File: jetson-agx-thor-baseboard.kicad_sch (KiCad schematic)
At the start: 7 parts

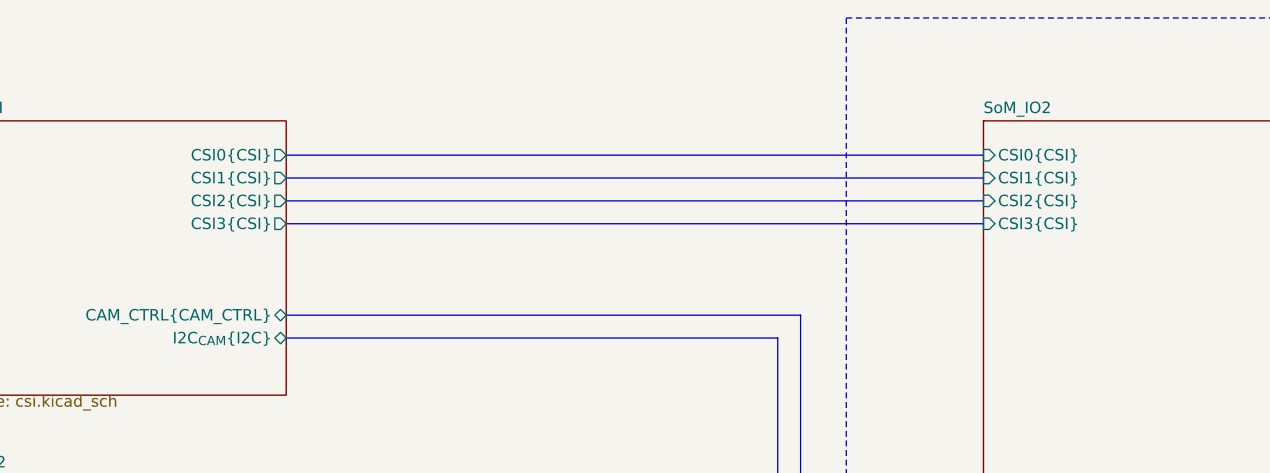
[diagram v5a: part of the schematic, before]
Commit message: [#85326] Update CSI naming convention
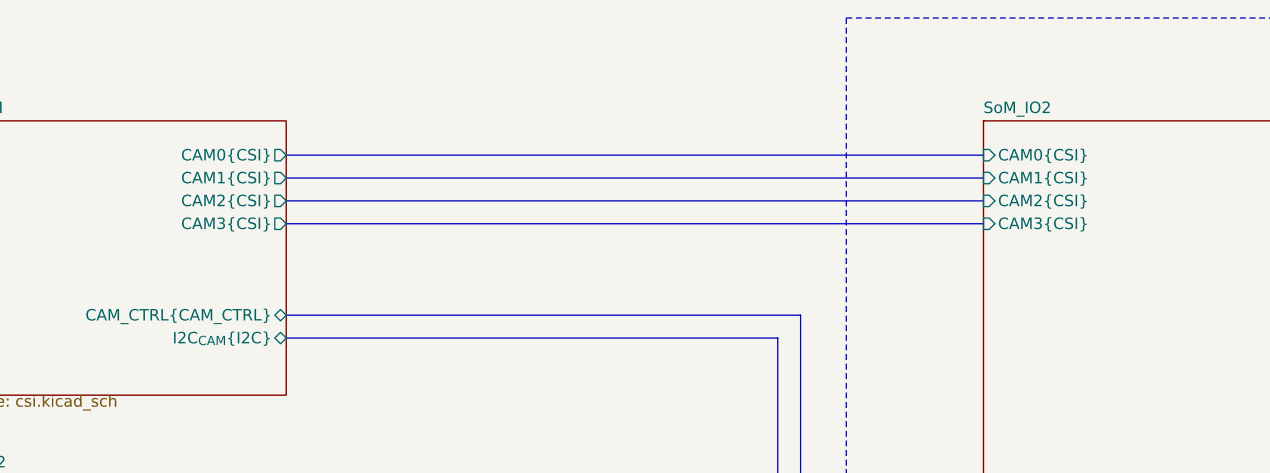
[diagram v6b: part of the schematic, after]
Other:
- sheet CSI ports: added CAM0{CSI}, CAM1{CSI}, CAM2{CSI}, CAM3{CSI}; removed CSI0{CSI}, CSI1{CSI}, CSI2{CSI}, CSI3{CSI}
- sheet SoM_IO2 ports: added CAM0{CSI}, CAM1{CSI}, CAM2{CSI}, CAM3{CSI}; removed CSI0{CSI}, CSI1{CSI}, CSI2{CSI}, CSI3{CSI}
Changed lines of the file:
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@@
-			)
-		)
-		(pin "CSI0{CSI}" output
-			(at 100.33 36.83 0)
-			(effects
-				(font
-					(size 1.27 1.27)
-				)
-				(justify right)
-			)
-		)
-		(pin "CSI1{CSI}" output
-			(at 100.33 39.37 0)
-			(effects
-				(font
-					(size 1.27 1.27)
-				)
-				(justify right)
-			)
-		)
-		(pin "CSI2{CSI}" output
-			(at 100.33 41.91 0)
-			(effects
-				(font
-					(size 1.27 1.27)
-				)
-				(justify right)
-			)
-		)
-		(pin "CSI3{CSI}" output
-			(at 100.33 44.45 0)
-			(effects
-				(font
-					(size 1.27 1.27)
-				)
-				(justify right)
 			)
 		)
@@
 		(pin "CAM_CTRL{CAM_CTRL}" bidirectional
 			(at 100.33 54.61 0)
+			(effects
+				(font
+					(size 1.27 1.27)
+				)
+				(justify right)
+			)
+		)
+		(pin "CAM0{CSI}" output
+			(at 100.33 36.83 0)
+			(effects
+				(font
+					(size 1.27 1.27)
+				)
+				(justify right)
+			)
+		)
+		(pin "CAM1{CSI}" output
+			(at 100.33 39.37 0)
+			(effects
+				(font
+					(size 1.27 1.27)
+				)
+				(justify right)
+			)
+		)
+		(pin "CAM2{CSI}" output
+			(at 100.33 41.91 0)
+			(effects
+				(font
+					(size 1.27 1.27)
+				)
+				(justify right)
+			)
+		)
+		(pin "CAM3{CSI}" output
+			(at 100.33 44.45 0)
 			(effects
 				(font
@@
 			)
 		)
-		(pin "CSI0{CSI}" input
-			(at 177.8 36.83 180)
-			(effects
-				(font
-					(size 1.27 1.27)
-				)
-				(justify left)
-			)
-		)
-		(pin "CSI1{CSI}" input
-			(at 177.8 39.37 180)
-			(effects
-				(font
-					(size 1.27 1.27)
-				)
-				(justify left)
-			)
-		)
-		(pin "CSI2{CSI}" input
-			(at 177.8 41.91 180)
-			(effects
-				(font
-					(size 1.27 1.27)
-				)
-				(justify left)
-			)
-		)
-		(pin "CSI3{CSI}" input
-			(at 177.8 44.45 180)
-			(effects
-				(font
-					(size 1.27 1.27)
-				)
-				(justify left)
-			)
-		)
 		(pin "PCIe_{C3x2}{PCIe}" bidirectional
 			(at 177.8 106.68 180)
@@
 			(effects
 				(font
+					(size 1.27 1.27)
+				)
+				(justify left)
+			)
+		)
+		(pin "CAM1{CSI}" input
+			(at 177.8 39.37 180)
+			(effects
+				(font
+					(size 1.27 1.27)
+				)
+				(justify left)
+			)
+		)
+		(pin "CAM0{CSI}" input
+			(at 177.8 36.83 180)
+			(effects
+				(font
+					(size 1.27 1.27)
+				)
+				(justify left)
+			)
+		)
+		(pin "CAM2{CSI}" input
+			(at 177.8 41.91 180)
+			(effects
+				(font
+					(size 1.27 1.27)
+				)
+				(justify left)
+			)
+		)
+		(pin "CAM3{CSI}" input
+			(at 177.8 44.45 180)
+			(effects
+				(font

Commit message: [#85326] Clean DRC
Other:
- sheet SoM_IO ports: added none; removed I2C_CONN_PEN
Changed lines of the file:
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@@
-			)
-		)
-		(pin "I2C_CONN_PEN" output
-			(at 254 198.12 0)
-			(effects
-				(font
-					(size 1.27 1.27)
-				)
-				(justify right)
 			)
 		)

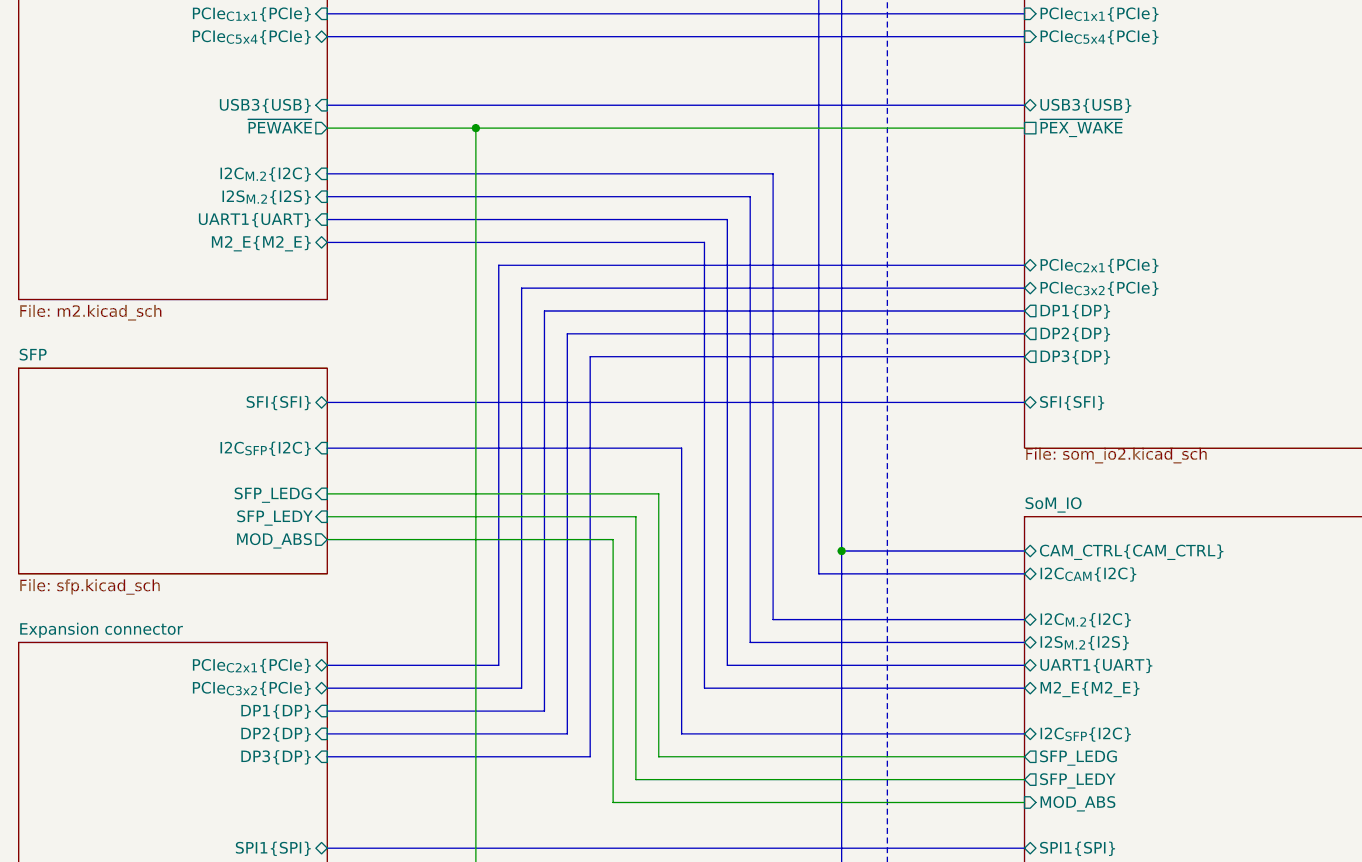
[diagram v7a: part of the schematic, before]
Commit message: [#85326] Remove auxilary M.2 Key E interfaces
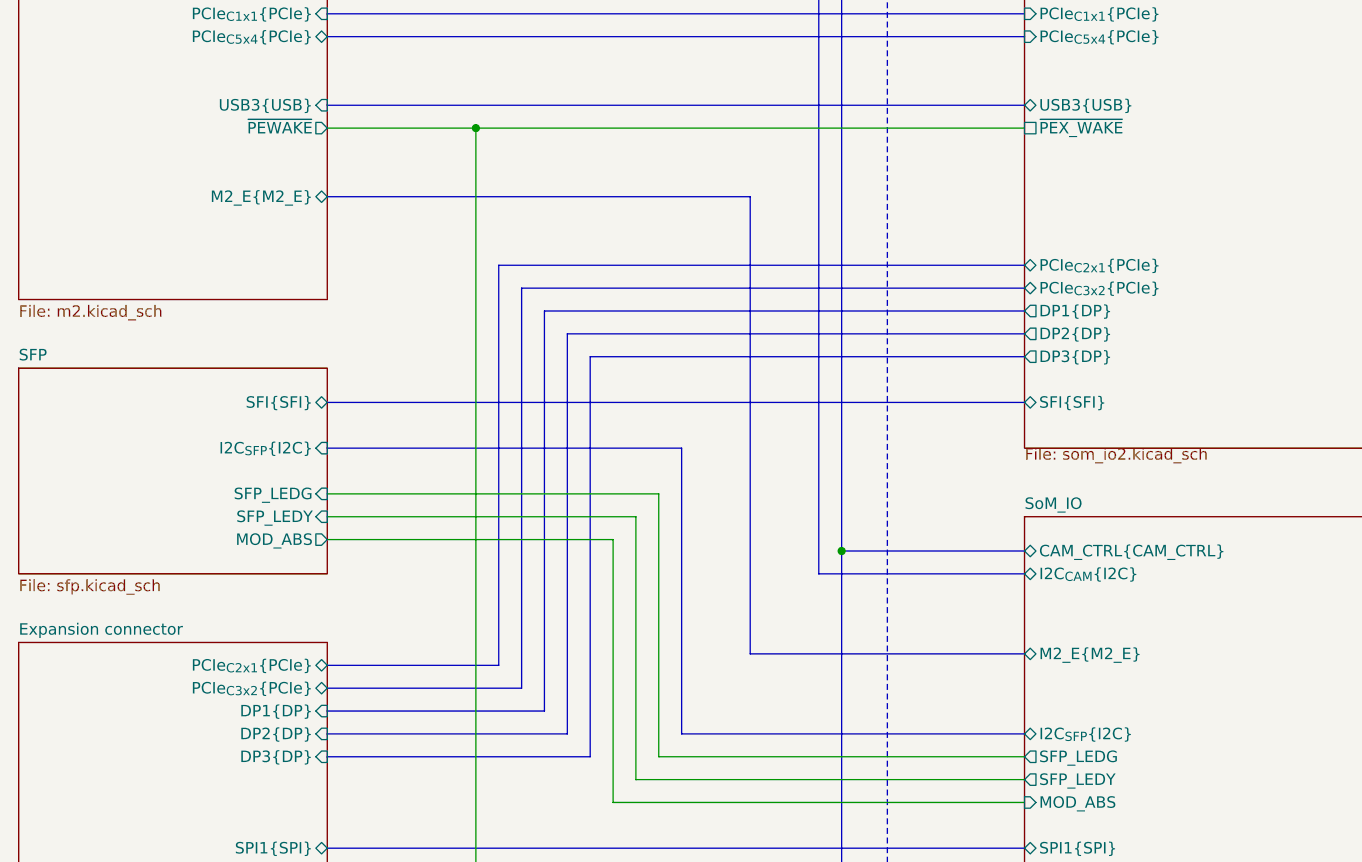
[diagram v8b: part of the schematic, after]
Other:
- sheet M.2 ports: added none; removed I2C_{M.2}{I2C}, I2S_{M.2}{I2S}, UART1{UART}
- sheet SoM_IO ports: added none; removed I2C_{M.2}{I2C}, I2S_{M.2}{I2S}, UART1{UART}
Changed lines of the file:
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@@
 	(bus
 		(pts
-			(xy 177.8 151.13) (xy 142.24 151.13)
+			(xy 177.8 147.32) (xy 147.32 147.32)
 		)
 		(stroke
@@
 		)
 	)
-	(bus
-		(pts
-			(xy 100.33 93.98) (xy 149.86 93.98)
-		)
-		(stroke
-			(width 0)
-			(type default)
-		)
-	)
 	(wire
 		(pts
@@
 		)
 	)
-	(bus
-		(pts
-			(xy 100.33 99.06) (xy 144.78 99.06)
-		)
-		(stroke
-			(width 0)
-			(type default)
-			(color 255 153 0 1)
-		)
-	)
 	(wire
 		(pts
@@
 		)
 	)
-	(bus
-		(pts
-			(xy 177.8 143.51) (xy 149.86 143.51)
-		)
-		(stroke
-			(width 0)
-			(type default)
-		)
-	)
 	(wire
 		(pts
@@
 	(bus
 		(pts
-			(xy 142.24 151.13) (xy 142.24 101.6)
+			(xy 147.32 147.32) (xy 147.32 96.52)
 		)
 		(stroke
@@
 	(bus
 		(pts
-			(xy 100.33 96.52) (xy 147.32 96.52)
-		)
-		(stroke
-			(width 0)
-			(type default)
-		)
-	)
-	(bus
-		(pts
 			(xy 157.48 135.89) (xy 157.48 222.25)
 		)
@@
 	(bus
 		(pts
-			(xy 149.86 93.98) (xy 149.86 143.51)
-		)
-		(stroke
-			(width 0)
-			(type default)
-		)
-	)
-	(bus
-		(pts
 			(xy 100.33 168.91) (xy 177.8 168.91)
 		)
@@
 	(bus
 		(pts
-			(xy 142.24 101.6) (xy 100.33 101.6)
+			(xy 147.32 96.52) (xy 100.33 96.52)
 		)
 		(stroke
@@
 		)
 	)
-	(bus
-		(pts
-			(xy 177.8 146.05) (xy 147.32 146.05)
-		)
-		(stroke
-			(width 0)
-			(type default)
-		)
-	)
 	(wire
 		(pts
@@
 	(bus
 		(pts
-			(xy 177.8 148.59) (xy 144.78 148.59)
-		)
-		(stroke
-			(width 0)
-			(type default)
-			(color 255 153 0 1)
-		)
-	)
-	(bus
-		(pts
 			(xy 254 39.37) (xy 331.47 39.37)
 		)
@@
 	(bus
 		(pts
-			(xy 147.32 96.52) (xy 147.32 146.05)
-		)
-		(stroke
-			(width 0)
-			(type default)
-		)
-	)
-	(bus
-		(pts
 			(xy 100.33 41.91) (xy 177.8 41.91)
 		)
@@
 	(bus
 		(pts
-			(xy 144.78 99.06) (xy 144.78 148.59)
-		)
-		(stroke
-			(width 0)
-			(type default)
-			(color 255 153 0 1)
-		)
-	)
-	(bus
-		(pts
 			(xy 177.8 114.3) (xy 129.54 114.3)
 		)
@@
 			)
 		)
-		(pin "I2C_{M.2}{I2C}" input
-			(at 100.33 93.98 0)
-			(effects
-				(font
-					(size 1.27 1.27)
-				)
-				(justify right)
-			)
-		)
-		(pin "I2S_{M.2}{I2S}" input
-			(at 100.33 96.52 0)
-			(effects
-				(font
-					(size 1.27 1.27)
-				)
-				(justify right)
-			)
-		)
-		(pin "UART1{UART}" input
-			(at 100.33 99.06 0)
-			(effects
-				(font
-					(size 1.27 1.27)
-				)
-				(justify right)
-			)
-		)
 		(pin "~{PEWAKE}" output
 			(at 100.33 88.9 0)
@@
 		)
 		(pin "M2_E{M2_E}" bidirectional
-			(at 100.33 101.6 0)
+			(at 100.33 96.52 0)
 			(effects
 				(font
@@
 			)
 		)
-		(pin "UART1{UART}" bidirectional
-			(at 177.8 148.59 180)
-			(effects
-				(font
-					(size 1.27 1.27)
-				)
-				(justify left)
-			)
-		)
 		(pin "FAN_PWM" output
 			(at 254 208.28 0)
@@
 			)
 		)
-		(pin "I2C_{M.2}{I2C}" bidirectional
-			(at 177.8 143.51 180)
-			(effects
-				(font
-					(size 1.27 1.27)
-				)
-				(justify left)
-			)
-		)
 		(pin "I2C_{SYS}{I2C}" bidirectional
 			(at 177.8 181.61 180)
@@
 			)
 		)
-		(pin "I2S_{M.2}{I2S}" bidirectional
-			(at 177.8 146.05 180)
-			(effects
-				(font
-					(size 1.27 1.27)
-				)
-				(justify left)
-			)
-		)
 		(pin "I2C_{CONN}{I2C}" bidirectional
 			(at 254 195.58 0)
@@
 		)
 		(pin "M2_E{M2_E}" bidirectional
-			(at 177.8 151.13 180)
+			(at 177.8 147.32 180)
 			(effects
 				(font
